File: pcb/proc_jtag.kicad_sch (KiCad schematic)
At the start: 23 parts, among them SW1 SW_Push, U1 XC6SLX16-FTG256, U11 74LVC1G08, U15 BCM56DS, U16 74LVC1G32, U17 74LS04, U18 74LS08, U19 LMC555xMM

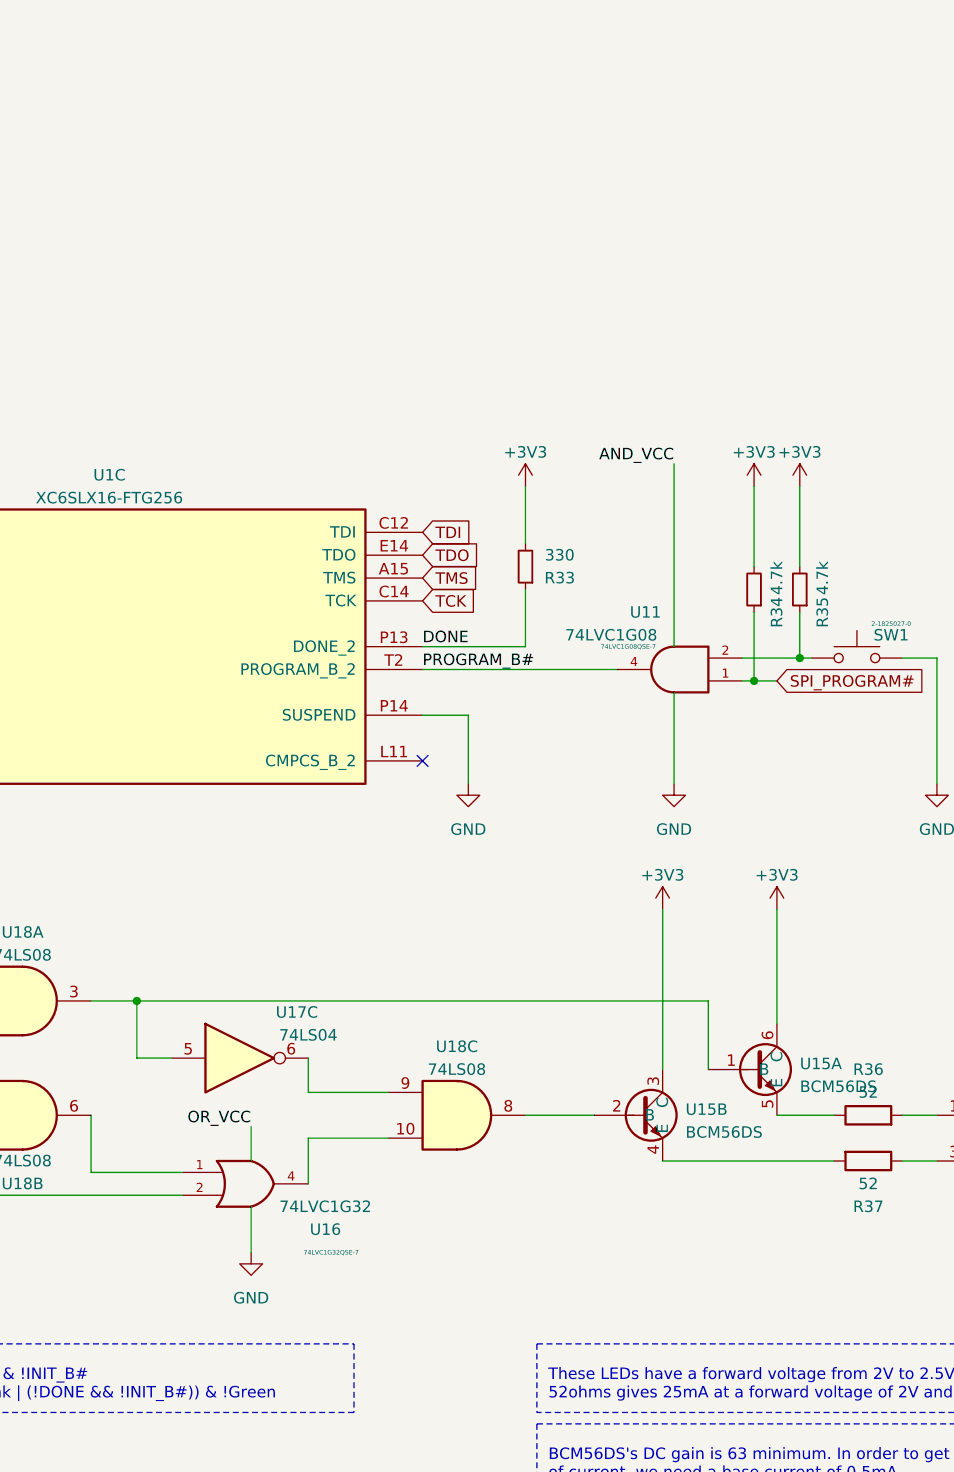
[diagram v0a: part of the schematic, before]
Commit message: place components relative to each others
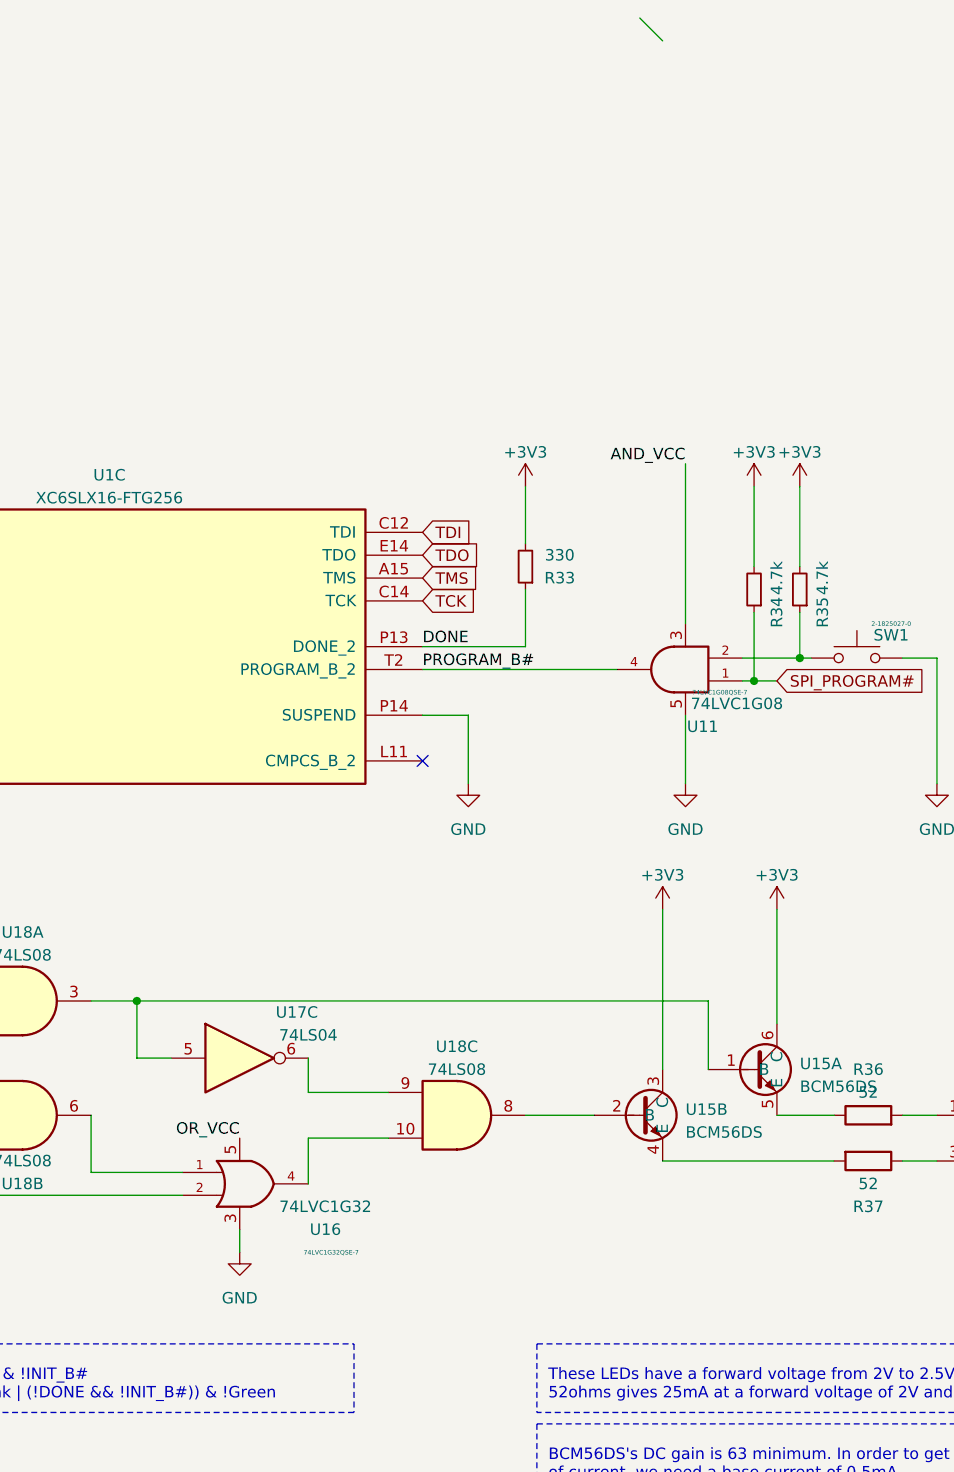
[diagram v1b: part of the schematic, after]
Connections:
- net +3V3: no longer C71.2, C91.2, C92.2, C93.2, C94.1, C95.2, C96.2, D3.2 (K), SW1.2, U1.P14 (SUSPEND), U11.5 (VCC), U16.3 (GND), U17.7 (GND), U18.7 (GND), U19.1 (GND)
- new net GND: C71.2, C91.2, C92.2, C93.2, C94.1, C95.2, C96.2, D3.2 (K), SW1.2, U1.P14 (SUSPEND), U11.5, U16.3, U17.7 (GND), U18.7 (GND), U19.1 (GND)

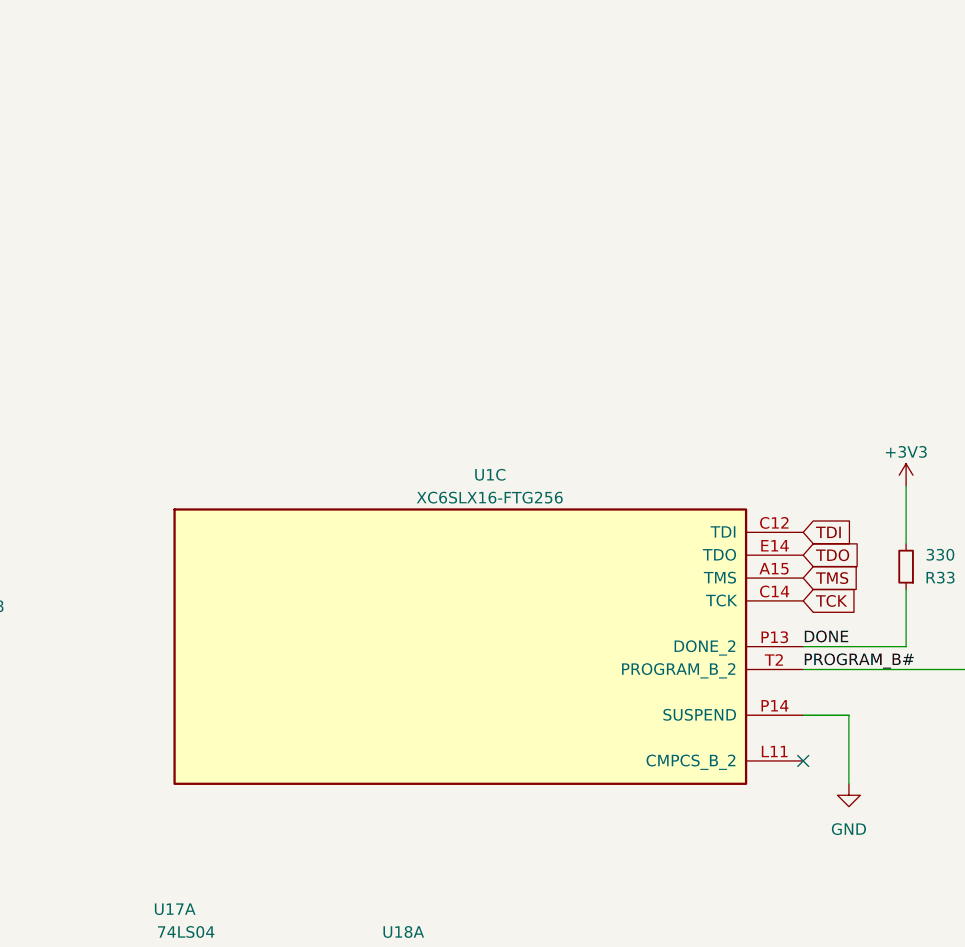
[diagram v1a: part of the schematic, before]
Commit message: change to lx9 and reduce power
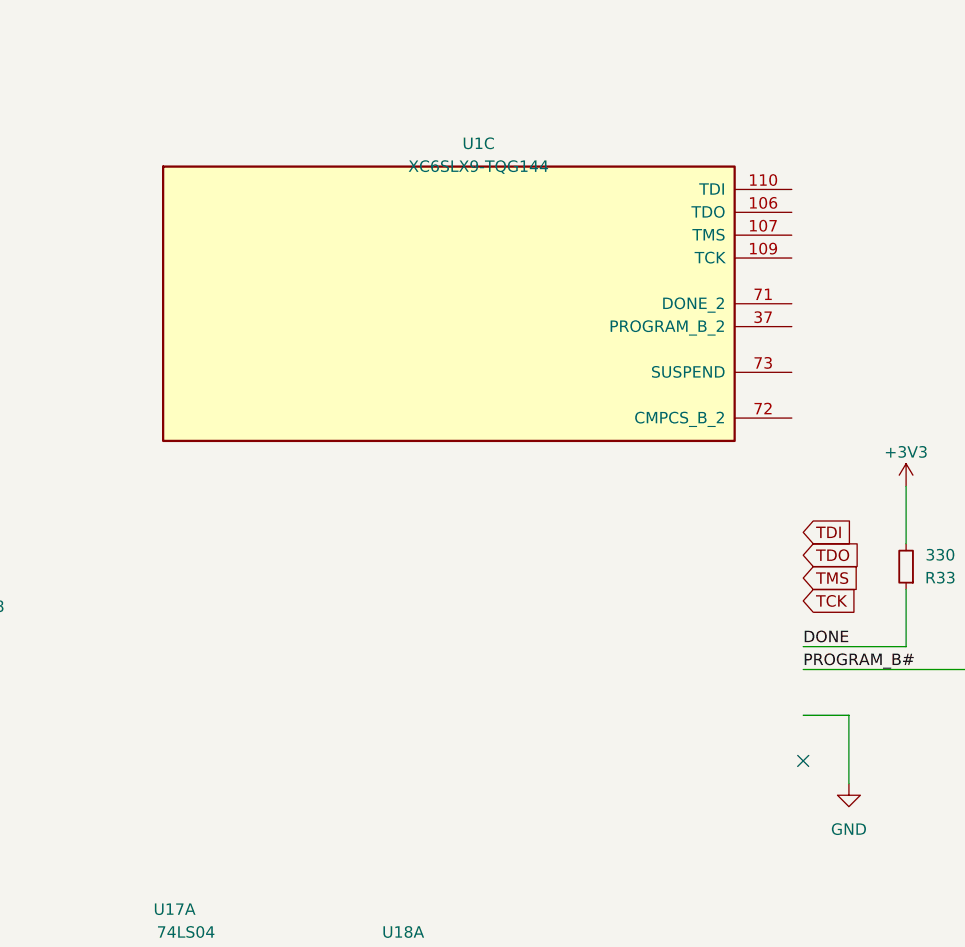
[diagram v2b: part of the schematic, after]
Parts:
- removed U1: XC6SLX16-FTG256, Package_BGA:Xilinx_FTG256, symbol FPGA_Xilinx_Spartan6:XC6SLX16-FTG256
- added U1: XC6SLX9-TQG144, Package_QFP:TQFP-144_20x20mm_P0.5mm, symbol FPGA_Xilinx_Spartan6:XC6SLX9-TQG144
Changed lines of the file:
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@@
     (pin "7")
   )
-  (symbol (lib_id "FPGA_Xilinx_Spartan6:XC6SLX16-FTG256") (at 154.94 53.34 0) (unit 3)
+  (symbol (lib_id "FPGA_Xilinx_Spartan6:XC6SLX9-TQG144") (at 153.67 15.24 0) (unit 3)
     (in_bom yes) (on_board yes) (fields_autoplaced)
-    (property "Reference" "U1" (id 0) (at 158.242 34.29 0))
-    (property "Value" "XC6SLX16-FTG256" (id 1) (at 158.242 36.83 0))
-    (property "Footprint" "Package_BGA:Xilinx_FTG256" (id 2) (at 154.94 53.34 0)
+    (property "Reference" "U1" (id 0) (at 156.972 -2.54 0))
+    (property "Value" "XC6SLX9-TQG144" (id 1) (at 156.972 0 0))
+    (property "Footprint" "Package_QFP:TQFP-144_20x20mm_P0.5mm" (id 2) (at 153.67 15.24 0)
       (effects (font (size 1.27 1.27)) hide)
     )
-    (property "Datasheet" "" (id 3) (at 154.94 53.34 0))
-    (pin "A15")
-    (pin "C12")
-    (pin "C14")
-    (pin "E14")
-    (pin "L11")
-    (pin "P13")
-    (pin "P14")
-    (pin "T2")
+    (property "Datasheet" "" (id 3) (at 153.67 15.24 0))
+    (pin "106")
+    (pin "107")
+    (pin "109")
+    (pin "110")
+    (pin "37")
+    (pin "71")
+    (pin "72")
+    (pin "73")
   )
 )

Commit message: route pol
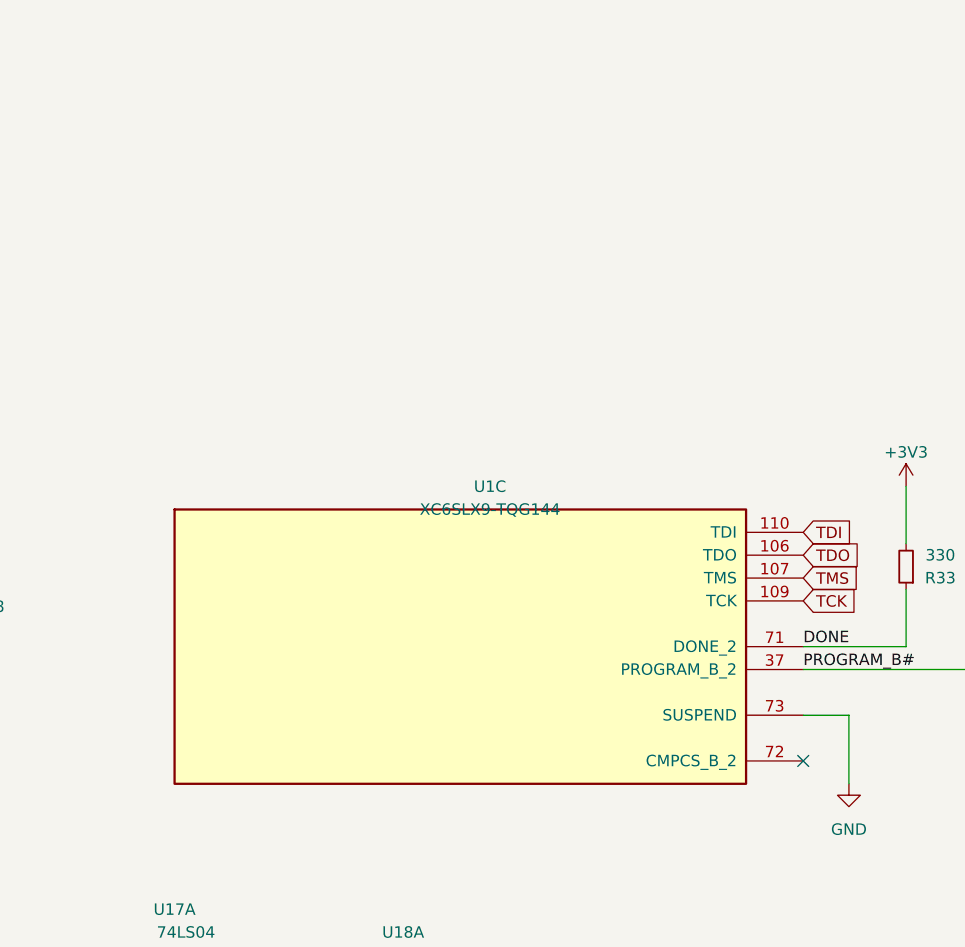
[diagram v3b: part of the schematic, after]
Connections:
- net DONE: now also U1.71 (DONE_2)
- net GND: now also U1.73 (SUSPEND)
- net PROGRAM_B#: now also U1.37 (PROGRAM_B_2)
- net TCK: now also U1.109 (TCK)
- net TDI: now also U1.110 (TDI)
- net TDO: now also U1.106 (TDO)
- net TMS: now also U1.107 (TMS)
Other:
- moved on the sheet: U1C
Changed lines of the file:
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@@
     (pin "7")
   )
-  (symbol (lib_id "FPGA_Xilinx_Spartan6:XC6SLX9-TQG144") (at 153.67 15.24 0) (unit 3)
+  (symbol (lib_id "FPGA_Xilinx_Spartan6:XC6SLX9-TQG144") (at 154.94 53.34 0) (unit 3)
     (in_bom yes) (on_board yes) (fields_autoplaced)
-    (property "Reference" "U1" (id 0) (at 156.972 -2.54 0))
-    (property "Value" "XC6SLX9-TQG144" (id 1) (at 156.972 0 0))
-    (property "Footprint" "Package_QFP:TQFP-144_20x20mm_P0.5mm" (id 2) (at 153.67 15.24 0)
+    (property "Reference" "U1" (id 0) (at 158.242 35.56 0))
+    (property "Value" "XC6SLX9-TQG144" (id 1) (at 158.242 38.1 0))
+    (property "Footprint" "Package_QFP:TQFP-144_20x20mm_P0.5mm" (id 2) (at 154.94 53.34 0)
       (effects (font (size 1.27 1.27)) hide)
     )
-    (property "Datasheet" "" (id 3) (at 153.67 15.24 0))
+    (property "Datasheet" "" (id 3) (at 154.94 53.34 0))
     (pin "106")
     (pin "107")

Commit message: start the routing
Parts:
- added C20, C21: 0.1uF, Capacitor_SMD:C_0402_1005Metric, symbol Device:C_Small
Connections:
- net +3V3: now also C20.1, C21.1
- net GND: now also C20.2, C21.2
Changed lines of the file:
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@@
-(kicad_sch (version 20210406) (generator eeschema)
+(kicad_sch (version 20210621) (generator eeschema)
   (paper "User" 299.999 180.01)
   (junction (at 24.13 24.13) (diameter 0.9144) (color 0 0 0 0))
@@
   (junction (at 24.13 96.52) (diameter 0.9144) (color 0 0 0 0))
   (junction (at 24.13 120.65) (diameter 0.9144) (color 0 0 0 0))
+  (junction (at 24.13 146.05) (diameter 0.9144) (color 0 0 0 0))
+  (junction (at 24.13 153.67) (diameter 0.9144) (color 0 0 0 0))
+  (junction (at 34.29 146.05) (diameter 0.9144) (color 0 0 0 0))
   (junction (at 73.66 85.09) (diameter 0.9144) (color 0 0 0 0))
   (junction (at 91.44 97.79) (diameter 0.9144) (color 0 0 0 0))
@@
     (stroke (width 0) (type solid) (color 0 0 0 0))
   )
+  (wire (pts (xy 24.13 144.78) (xy 24.13 146.05))
+    (stroke (width 0) (type solid) (color 0 0 0 0))
+  )
+  (wire (pts (xy 24.13 146.05) (xy 24.13 147.32))
+    (stroke (width 0) (type solid) (color 0 0 0 0))
+  )
+  (wire (pts (xy 24.13 146.05) (xy 34.29 146.05))
+    (stroke (width 0) (type solid) (color 0 0 0 0))
+  )
+  (wire (pts (xy 24.13 152.4) (xy 24.13 153.67))
+    (stroke (width 0) (type solid) (color 0 0 0 0))
+  )
+  (wire (pts (xy 24.13 153.67) (xy 24.13 154.94))
+    (stroke (width 0) (type solid) (color 0 0 0 0))
+  )
+  (wire (pts (xy 24.13 153.67) (xy 34.29 153.67))
+    (stroke (width 0) (type solid) (color 0 0 0 0))
+  )
+  (wire (pts (xy 34.29 146.05) (xy 34.29 147.32))
+    (stroke (width 0) (type solid) (color 0 0 0 0))
+  )
+  (wire (pts (xy 34.29 146.05) (xy 40.64 146.05))
+    (stroke (width 0) (type solid) (color 0 0 0 0))
+  )
+  (wire (pts (xy 34.29 152.4) (xy 34.29 153.67))
+    (stroke (width 0) (type solid) (color 0 0 0 0))
+  )
   (wire (pts (xy 52.07 100.33) (xy 52.07 106.68))
     (stroke (width 0) (type solid) (color 0 0 0 0))
@@
     (effects (font (size 1.27 1.27)) (justify left bottom))
   )
+  (label "MOSFET_VCC" (at 40.64 146.05 0)
+    (effects (font (size 1.27 1.27)) (justify left bottom))
+  )
   (label "NOT_VCC" (at 68.58 34.29 180)
     (effects (font (size 1.27 1.27)) (justify right bottom))
@@
     (effects (font (size 1.27 1.27)) (justify left bottom))
   )
+  (label "MOSFET_VCC" (at 219.71 82.55 180)
+    (effects (font (size 1.27 1.27)) (justify right bottom))
+  )
   (label "AND_VCC" (at 222.25 33.02 180)
     (effects (font (size 1.27 1.27)) (justify right bottom))
+  )
+  (label "MOSFET_VCC" (at 232.41 82.55 0)
+    (effects (font (size 1.27 1.27)) (justify left bottom))
   )
   (global_label "INIT_B#" (shape input) (at 107.95 92.71 180) (fields_autoplaced)
@@
     (pin "1")
   )
+  (symbol (lib_id "power:+3V3") (at 24.13 144.78 0) (unit 1)
+    (in_bom yes) (on_board yes) (fields_autoplaced)
+    (property "Reference" "#PWR0108" (id 0) (at 24.13 148.59 0)
+      (effects (font (size 1.27 1.27)) hide)
+    )
+    (property "Value" "+3V3" (id 1) (at 24.13 140.97 0))
+    (property "Footprint" "" (id 2) (at 24.13 144.78 0)
+      (effects (font (size 1.27 1.27)) hide)
+    )
+    (property "Datasheet" "" (id 3) (at 24.13 144.78 0)
+      (effects (font (size 1.27 1.27)) hide)
+    )
+    (pin "1")
+  )
   (symbol (lib_id "power:+3V3") (at 58.42 82.55 0) (unit 1)
     (in_bom yes) (on_board yes) (fields_autoplaced)
@@
     (pin "1")
   )
-  (symbol (lib_id "power:+3V3") (at 219.71 82.55 0) (unit 1)
-    (in_bom yes) (on_board yes) (fields_autoplaced)
-    (property "Reference" "#PWR0109" (id 0) (at 219.71 86.36 0)
-      (effects (font (size 1.27 1.27)) hide)
-    )
-    (property "Value" "+3V3" (id 1) (at 219.71 78.74 0))
-    (property "Footprint" "" (id 2) (at 219.71 82.55 0)
-      (effects (font (size 1.27 1.27)) hide)
-    )
-    (property "Datasheet" "" (id 3) (at 219.71 82.55 0)
-      (effects (font (size 1.27 1.27)) hide)
-    )
-    (pin "1")
-  )
   (symbol (lib_id "power:+3V3") (at 229.87 35.56 0) (unit 1)
     (in_bom yes) (on_board yes) (fields_autoplaced)
@@
     (pin "1")
   )
-  (symbol (lib_id "power:+3V3") (at 232.41 82.55 0) (unit 1)
-    (in_bom yes) (on_board yes) (fields_autoplaced)
-    (property "Reference" "#PWR0108" (id 0) (at 232.41 86.36 0)
-      (effects (font (size 1.27 1.27)) hide)
-    )
-    (property "Value" "+3V3" (id 1) (at 232.41 78.74 0))
-    (property "Footprint" "" (id 2) (at 232.41 82.55 0)
-      (effects (font (size 1.27 1.27)) hide)
-    )
-    (property "Datasheet" "" (id 3) (at 232.41 82.55 0)
-      (effects (font (size 1.27 1.27)) hide)
-    )
-    (pin "1")
-  )
   (symbol (lib_id "power:+3V3") (at 234.95 35.56 0) (unit 1)
     (in_bom yes) (on_board yes) (fields_autoplaced)
@@
     )
     (property "Datasheet" "" (id 3) (at 24.13 129.54 0)
+      (effects (font (size 1.27 1.27)) hide)
+    )
+    (pin "1")
+  )
+  (symbol (lib_id "power:GND") (at 24.13 154.94 0) (unit 1)
+    (in_bom yes) (on_board yes) (fields_autoplaced)
+    (property "Reference" "#PWR0109" (id 0) (at 24.13 161.29 0)
+      (effects (font (size 1.27 1.27)) hide)
+    )
+    (property "Value" "GND" (id 1) (at 24.13 160.02 0))
+    (property "Footprint" "" (id 2) (at 24.13 154.94 0)
+      (effects (font (size 1.27 1.27)) hide)
+    )
+    (property "Datasheet" "" (id 3) (at 24.13 154.94 0)
       (effects (font (size 1.27 1.27)) hide)
     )
@@
       (effects (font (size 1.27 1.27)) hide)
     )
+    (pin "1")
+    (pin "2")
+  )
+  (symbol (lib_id "Device:C_Small") (at 24.13 149.86 0) (unit 1)
+    (in_bom yes) (on_board yes) (fields_autoplaced)
+    (property "Reference" "C20" (id 0) (at 26.67 149.2249 0)
+      (effects (font (size 1.27 1.27)) (justify left))
+    )
+    (property "Value" "0.1uF" (id 1) (at 26.67 151.7649 0)
+      (effects (font (size 1.27 1.27)) (justify left))
+    )
+    (property "Footprint" "Capacitor_SMD:C_0402_1005Metric" (id 2) (at 24.13 149.86 0)
+      (effects (font (size 1.27 1.27)) hide)
+    )
+    (property "Datasheet" "~" (id 3) (at 24.13 149.86 0)
+      (effects (font (size 1.27 1.27)) hide)
+    )
+    (pin "1")
+    (pin "2")
+  )
+  (symbol (lib_id "Device:C_Small") (at 34.29 149.86 0) (unit 1)
+    (in_bom yes) (on_board yes) (fields_autoplaced)
+    (property "Reference" "C21" (id 0) (at 36.83 149.2249 0)
+      (effects (font (size 1.27 1.27)) (justify left))
+    )
+    (property "Value" "0.1uF" (id 1) (at 36.83 151.7649 0)
+      (effects (font (size 1.27 1.27)) (justify left))
+    )
+    (property "Footprint" "Capacitor_SMD:C_0402_1005Metric" (id 2) (at 34.29 149.86 0)
+      (effects (font (size 1.27 1.27)) hide)
+    )
+    (property "Datasheet" "~" (id 3) (at 34.29 149.86 0)
+      (effects (font (size 1.27 1.27)) hide)
+    )
